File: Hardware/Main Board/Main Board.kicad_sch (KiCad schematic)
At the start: 56 parts, among them J1 Micro_SD_Card_Det1, J2 Camera Module, J3 Conn_01x09_Socket, J4 MIC 1 Connector, J5 MIC 2 Connector, J6 USB_C_Receptacle_USB2.0_16P, J7 OLED, U1 ESP32-S3-WROOM-2, U2 TPS63060, U3 TP4056-42-ESOP8

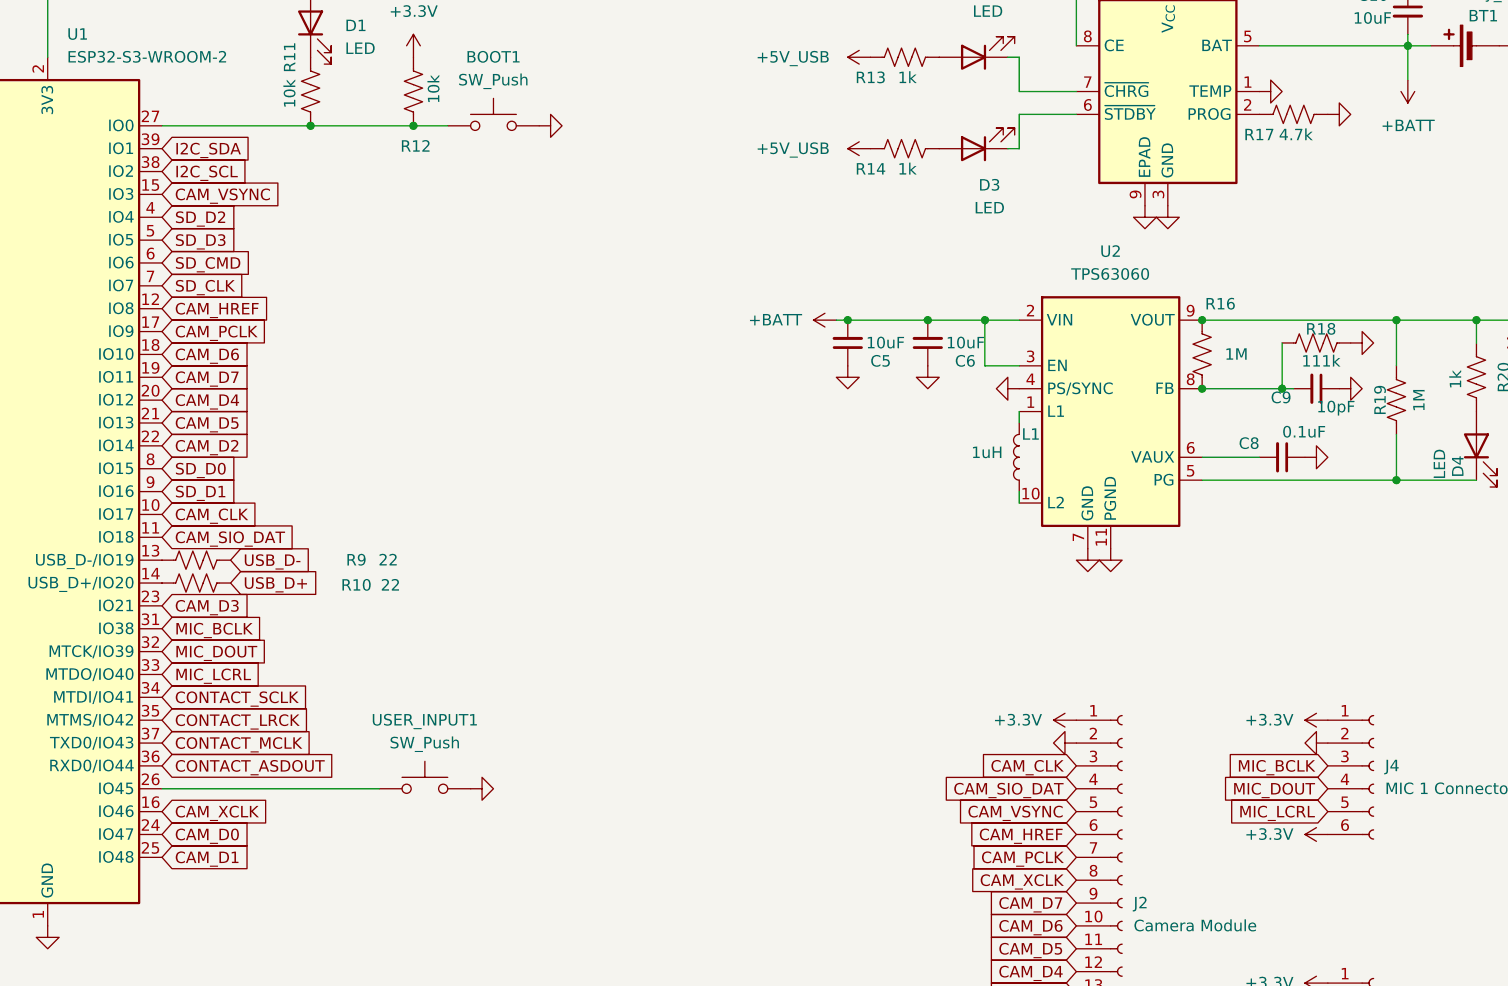
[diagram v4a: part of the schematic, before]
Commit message: revised main board layout, rearranged around strapping pins, rererouted for noise
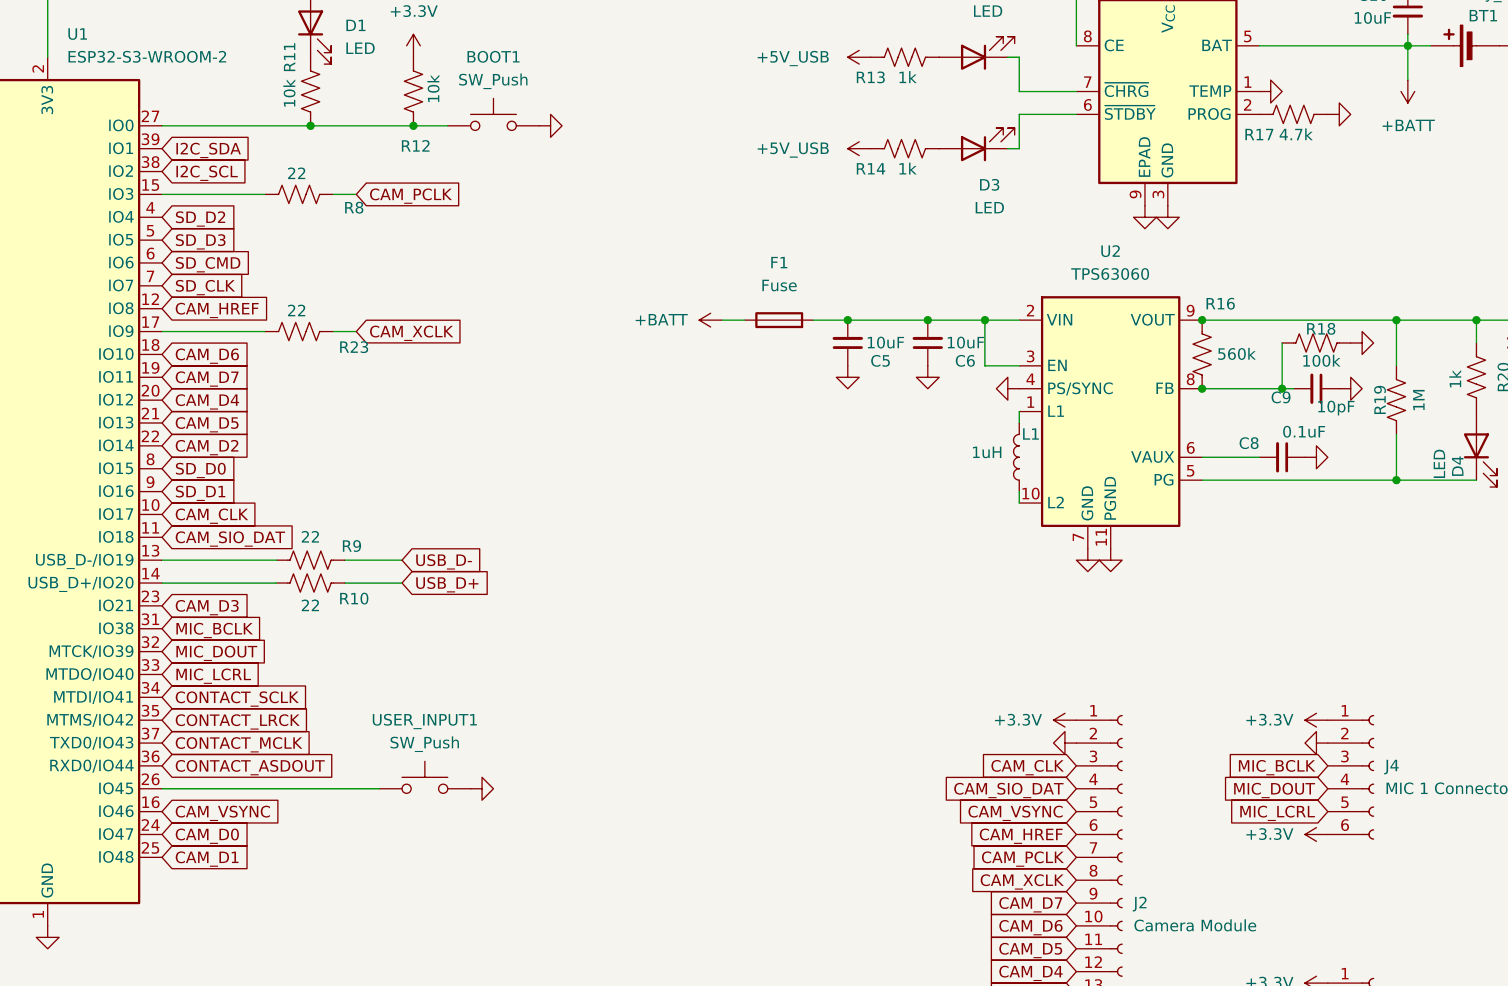
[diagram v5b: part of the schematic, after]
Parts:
- added F1: Fuse, Fuse:Fuse_1206_3216Metric, symbol Device:Fuse
- added R23, R8: 22, Resistor_SMD:R_0201_0603Metric, symbol Device:R_US
- R16: value 1M -> 560k
- R18: value 111k -> 100k
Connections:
- net +BATT: now also F1.1; no longer C5.2, C6.2, U2.2 (VIN), U2.3 (EN)
- net CAM_PCLK: now also R8.2; no longer U1.17 (IO9)
- net CAM_VSYNC: now also U1.16 (IO46); no longer U1.15 (IO3)
- net CAM_XCLK: now also R23.2; no longer U1.16 (IO46)
- new net: R8.1, U1.15 (IO3)
- new net: R23.1, U1.17 (IO9)
- new net: C5.2, C6.2, F1.2, U2.2 (VIN), U2.3 (EN)
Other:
- moved on the sheet: R10, R9

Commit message: reviewed most of main board, getting ready to finalize and prepare for manufacturing
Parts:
- added D5: SS14, Diode_SMD:D_SMA, symbol Diode:SS14
- added H1, H2: MountingHole, MountingHole:MountingHole_2.1mm, symbol Mechanical:MountingHole
- added Q1: AO3401A, Package_TO_SOT_SMD:SOT-23, symbol Transistor_FET:AO3401A
- added R24: 100k, Resistor_SMD:R_0402_1005Metric, symbol Device:R_US
- added TP4, TP5: TestPoint, TestPoint:TestPoint_Pad_1.0x1.0mm, symbol Connector:TestPoint
- C1, C10, C2, C3, C7, C8, C9: footprint Capacitor_SMD:C_01005_0402Metric -> Capacitor_SMD:C_0402_1005Metric
- C11, C12, C13: footprint Capacitor_SMD:C_01005_0402Metric -> Capacitor_SMD:C_0805_2012Metric
- C4, C5, C6: footprint Capacitor_SMD:C_01005_0402Metric -> Capacitor_SMD:C_0603_1608Metric
- D1, D2, D3, D4: footprint LED_SMD:LED_0201_0603Metric -> LED_SMD:LED_0603_1608Metric
- L1: footprint Inductor_SMD:L_0603_1608Metric -> Inductor_SMD:L_Bourns-SRN4018
- R1, R10, R11, R12, R13, R14, R15, R16, R17, R18, R19, R2, R20, R21, R22, R23, R3, R4, R5, R6, R7, R8, R9: footprint Resistor_SMD:R_0201_0603Metric -> Resistor_SMD:R_0402_1005Metric
- TP1, TP2, TP3: footprint TestPoint:TestPoint_Pad_D1.0mm -> Connector_PinHeader_2.54mm:PinHeader_1x01_P2.54mm_Vertical
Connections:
- net +5V_USB: now also D5.2 (A), Q1.1 (G), R24.1
- net +BATT: now also Q1.3 (D), TP5.1; no longer F1.1
- net CAM_VSYNC: now also U1.15 (IO3); no longer U1.16 (IO46)
- net GND: now also R24.2
- net at R8.1: now also U1.16 (IO46); no longer U1.15 (IO3)
- new net VIN: D5.1 (K), F1.1, Q1.2 (S), TP4.1
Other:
- moved on the sheet: R8

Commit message: fixed sd card, checked manufacturing feasibility and cleaned up board layout
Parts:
- added TP6: TestPoint, TestPoint:TestPoint_Pad_1.0x1.0mm, symbol Connector:TestPoint
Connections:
- net SD_CLK: now also U1.6 (IO6); no longer U1.7 (IO7)
- net SD_CMD: now also U1.7 (IO7); no longer U1.6 (IO6)
- net SD_D0: now also U1.5 (IO5); no longer U1.8 (IO15)
- net SD_D1: now also U1.4 (IO4); no longer U1.9 (IO16)
- net SD_D2: now also U1.9 (IO16); no longer U1.4 (IO4)
- net SD_D3: now also U1.8 (IO15); no longer U1.5 (IO5)
- net at J1.9 (DET): now also TP6.1
- net USB_D+ renamed D+
- net USB_D- renamed D-
- no-connect marks 3 -> 2
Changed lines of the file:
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@@
 	)
 	(no_connect
-		(at 62.23 184.15)
-	)
-	(no_connect
 		(at 256.54 29.21)
 	)
@@
 	(wire
 		(pts
-			(xy 50.8 156.21) (xy 50.8 161.29)
+			(xy 80.01 97.79) (xy 86.36 97.79)
 		)
 		(stroke
@@
 	(wire
 		(pts
-			(xy 250.19 59.69) (xy 256.54 59.69)
+			(xy 50.8 156.21) (xy 50.8 161.29)
 		)
 		(stroke
@@
 	(wire
 		(pts
-			(xy 151.13 68.58) (xy 151.13 73.66)
+			(xy 250.19 59.69) (xy 256.54 59.69)
 		)
 		(stroke
@@
 	(wire
 		(pts
-			(xy 22.86 168.91) (xy 26.67 168.91)
+			(xy 151.13 68.58) (xy 151.13 73.66)
 		)
 		(stroke
@@
 	(wire
 		(pts
-			(xy 87.63 46.99) (xy 91.44 46.99)
+			(xy 22.86 168.91) (xy 26.67 168.91)
 		)
 		(stroke
@@
 	(wire
 		(pts
-			(xy 256.54 45.72) (xy 256.54 46.99)
+			(xy 87.63 46.99) (xy 91.44 46.99)
 		)
 		(stroke
@@
 	(wire
 		(pts
-			(xy 33.02 27.94) (xy 33.02 31.75)
+			(xy 256.54 45.72) (xy 256.54 46.99)
 		)
 		(stroke
@@
 	(wire
 		(pts
-			(xy 86.36 97.79) (xy 80.01 97.79)
+			(xy 33.02 27.94) (xy 33.02 31.75)
 		)
 		(stroke
@@
 	(wire
 		(pts
-			(xy 256.54 44.45) (xy 256.54 45.72)
+			(xy 80.01 95.25) (xy 86.36 95.25)
 		)
 		(stroke
@@
 	(wire
 		(pts
-			(xy 82.55 123.19) (xy 78.74 123.19)
+			(xy 256.54 44.45) (xy 256.54 45.72)
 		)
 		(stroke
@@
 	(wire
 		(pts
-			(xy 72.39 95.25) (xy 59.69 95.25)
+			(xy 82.55 123.19) (xy 78.74 123.19)
 		)
 		(stroke
@@
 	(wire
 		(pts
-			(xy 86.36 95.25) (xy 80.01 95.25)
+			(xy 72.39 95.25) (xy 59.69 95.25)
 		)
 		(stroke
@@
 		)
 	)
-	(global_label "USB_D-"
-		(shape input)
+	(label "D+"
+		(at 242.57 40.64 0)
+		(effects
+			(font
+				(size 1.27 1.27)
+			)
+			(justify left bottom)
+		)
+	)
+	(label "D-"
 		(at 86.36 95.25 0)
-		(fields_autoplaced yes)
 		(effects
 			(font
 				(size 1.27 1.27)
 			)
-			(justify left)
+			(justify left bottom)
 		)
-		(property "Intersheetrefs" "${INTERSHEET_REFS}"
-			(at 96.9652 95.25 0)
-			(effects
-				(font
-					(size 1.27 1.27)
-				)
-				(justify left)
-				(hide yes)
+	)
+	(label "D-"
+		(at 242.57 45.72 0)
+		(effects
+			(font
+				(size 1.27 1.27)
+			)
+			(justify left bottom)
+		)
+	)
+	(label "D+"
+		(at 86.36 97.79 0)
+		(effects
+			(font
+				(size 1.27 1.27)
 			)
+			(justify left bottom)
 		)
 	)
@@
 	(global_label "SD_CMD"
 		(shape input)
-		(at 59.69 62.23 0)
+		(at 59.69 64.77 0)
 		(fields_autoplaced yes)
 		(effects
@@
 		)
 		(property "Intersheetrefs" "${INTERSHEET_REFS}"
-			(at 70.1137 62.23 0)
+			(at 70.1137 64.77 0)
 			(effects
 				(font
@@
 		)
 	)
-	(global_label "USB_D+"
-		(shape input)
-		(at 86.36 97.79 0)
-		(fields_autoplaced yes)
-		(effects
-			(font
-				(size 1.27 1.27)
-			)
-			(justify left)
-		)
-		(property "Intersheetrefs" "${INTERSHEET_REFS}"
-			(at 96.9652 97.79 0)
-			(effects
-				(font
-					(size 1.27 1.27)
-				)
-				(justify left)
-				(hide yes)
-			)
-		)
-	)
-	(global_label "USB_D+"
-		(shape input)
-		(at 242.57 40.64 180)
-		(fields_autoplaced yes)
-		(effects
-			(font
-				(size 1.27 1.27)
-			)
-			(justify right)
-		)
-		(property "Intersheetrefs" "${INTERSHEET_REFS}"
-			(at 231.9648 40.64 0)
-			(effects
-				(font
-					(size 1.27 1.27)
-				)
-				(justify right)
-				(hide yes)
-			)
-		)
-	)
 	(global_label "SD_D1"
 		(shape input)
@@
 	(global_label "SD_D0"
 		(shape input)
-		(at 59.69 85.09 0)
+		(at 59.69 59.69 0)
 		(fields_autoplaced yes)
 		(effects
@@
 		)
 		(property "Intersheetrefs" "${INTERSHEET_REFS}"
-			(at 68.6018 85.09 0)
+			(at 68.6018 59.69 0)
 			(effects
 				(font
@@
 		)
 	)
-	(global_label "USB_D-"
-		(shape input)
-		(at 242.57 45.72 180)
-		(fields_autoplaced yes)
-		(effects
-			(font
-				(size 1.27 1.27)
-			)
-			(justify right)
-		)
-		(property "Intersheetrefs" "${INTERSHEET_REFS}"
-			(at 231.9648 45.72 0)
-			(effects
-				(font
-					(size 1.27 1.27)
-				)
-				(justify right)
-				(hide yes)
-			)
-		)
-	)
 	(global_label "SD_CMD"
 		(shape input)
@@
 	(global_label "SD_CLK"
 		(shape input)
-		(at 59.69 64.77 0)
+		(at 59.69 62.23 0)
 		(fields_autoplaced yes)
 		(effects
@@
 		)
 		(property "Intersheetrefs" "${INTERSHEET_REFS}"
-			(at 69.6904 64.77 0)
+			(at 69.6904 62.23 0)
 			(effects
 				(font
@@
 	(global_label "SD_D2"
 		(shape input)
-		(at 59.69 57.15 0)
+		(at 59.69 87.63 0)
 		(fields_autoplaced yes)
 		(effects
@@
 		)
 		(property "Intersheetrefs" "${INTERSHEET_REFS}"
-			(at 68.6018 57.15 0)
+			(at 68.6018 87.63 0)
 			(effects
 				(font
@@
 	(global_label "SD_D1"
 		(shape input)
-		(at 59.69 87.63 0)
+		(at 59.69 57.15 0)
 		(fields_autoplaced yes)
 		(effects
@@
 		)
 		(property "Intersheetrefs" "${INTERSHEET_REFS}"
-			(at 68.6018 87.63 0)
+			(at 68.6018 57.15 0)
 			(effects
 				(font
@@
 	(global_label "SD_D3"
 		(shape input)
-		(at 59.69 59.69 0)
+		(at 59.69 85.09 0)
 		(fields_autoplaced yes)
 		(effects
@@
 		)
 		(property "Intersheetrefs" "${INTERSHEET_REFS}"
-			(at 68.6018 59.69 0)
+			(at 68.6018 85.09 0)
 			(effects
 				(font
@@
 					(unit 1)
 				)
+			)
+		)
+	)
+	(symbol
+		(lib_id "Connector:TestPoint")
+		(at 62.23 184.15 180)
+		(unit 1)
+		(exclude_from_sim no)
+		(in_bom yes)
+		(on_board yes)
+		(dnp no)
+		(property "Reference" "TP6"
+			(at 67.564 189.992 0)
+			(effects
+				(font
+					(size 1.27 1.27)
+				)
+				(justify left)
+			)
+		)
+		(property "Value" "TestPoint"
+			(at 59.69 186.1821 0)
+			(effects
+				(font
+					(size 1.27 1.27)
+				)
+				(justify left)
+				(hide yes)
+			)
+		)
+		(property "Footprint" "TestPoint:TestPoint_Pad_1.0x1.0mm"
+			(at 57.15 184.15 0)
+			(effects
+				(font
+					(size 1.27 1.27)
+				)
+				(hide yes)
+			)
+		)
+		(property "Datasheet" "~"
+			(at 57.15 184.15 0)
+			(effects
+				(font
+					(size 1.27 1.27)
+				)
+				(hide yes)
+			)
+		)
+		(property "Description" "test point"
+			(at 62.23 184.15 0)
+			(effects
+				(font
+					(size 1.27 1.27)
+				)
+				(hide yes)
+			)
+		)
+		(pin "1"
+		)
+		(instances
+			(project "Main Board"
+				(path "/06300a21-1646-41b0-b473-1c39557d6dab"
+					(reference "TP6")
+					(unit 1)
+				)
